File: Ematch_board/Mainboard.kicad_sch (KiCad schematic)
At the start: 69 parts, among them J10 Conn_01x02_Male, J11 Conn_Coaxial, J7 RBUS, J8 USB_C_Receptacle_USB2.0, J9 Conn_01x02_Male, Q1 MMDT2222A, U2 LTC4411, U3 RT9025-25GSP, U4 LTC4411, U5 SN65HVD230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

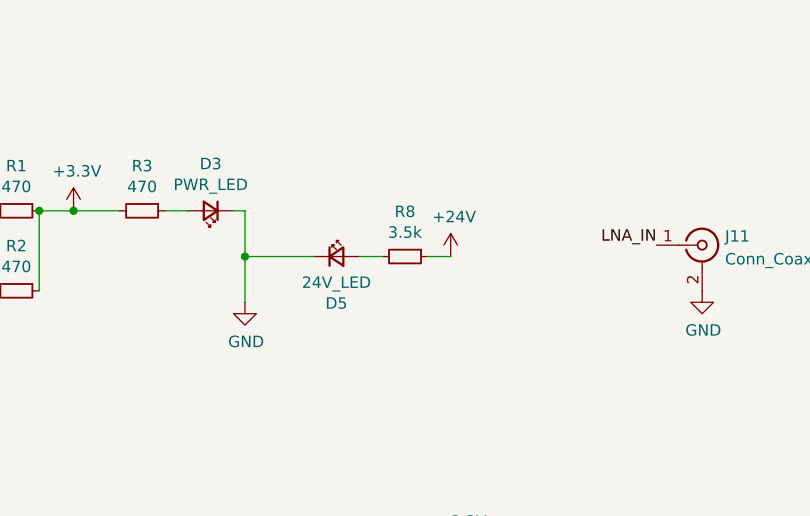
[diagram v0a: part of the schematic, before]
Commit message: Changed 24V LED resistor value
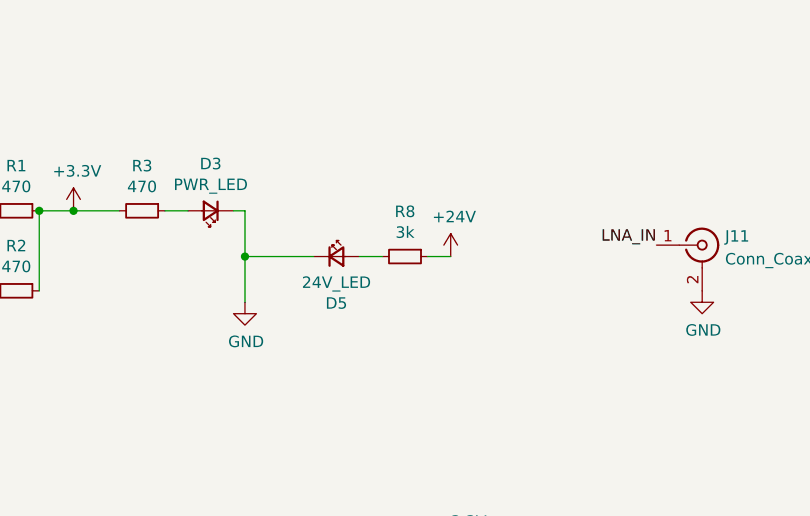
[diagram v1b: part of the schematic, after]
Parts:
- R8: value 3.5k -> 3k
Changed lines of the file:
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@@
     (in_bom yes) (on_board yes)
     (property "Reference" "R8" (id 0) (at 76.2 17.8816 90))
-    (property "Value" "3.5k" (id 1) (at 76.2 20.193 90))
+    (property "Value" "3k" (id 1) (at 76.2 20.193 90))
     (property "Footprint" "Resistor_SMD:R_0603_1608Metric" (id 2) (at 76.2 22.86 0)
       (effects (font (size 1.27 1.27)) hide)
@@
     )
     (path "/9f59f317-c728-437e-b7e8-8cd5c58754eb"
-      (reference "R8") (unit 1) (value "3.5k") (footprint "Resistor_SMD:R_0603_1608Metric")
+      (reference "R8") (unit 1) (value "3k") (footprint "Resistor_SMD:R_0603_1608Metric")
     )
     (path "/2e54b3a5-ce43-4593-88d5-e0f9c220138c"

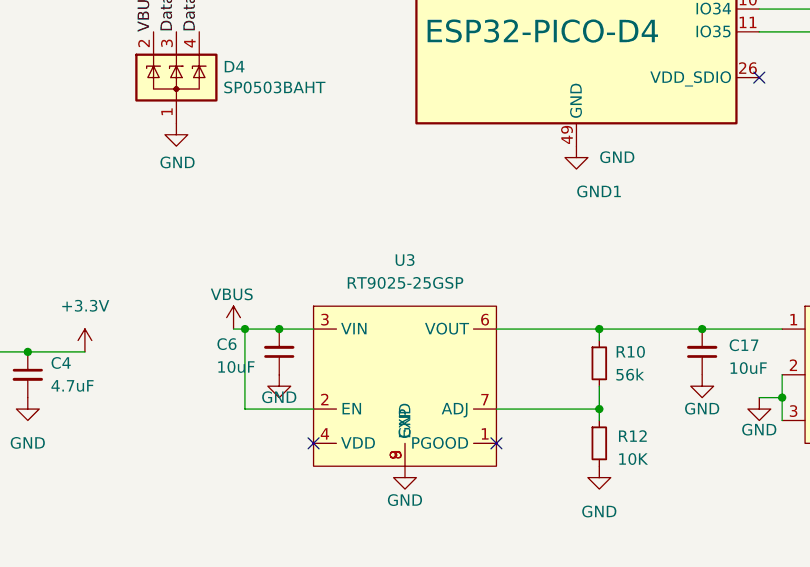
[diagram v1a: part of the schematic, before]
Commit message: Changed LDO symbol
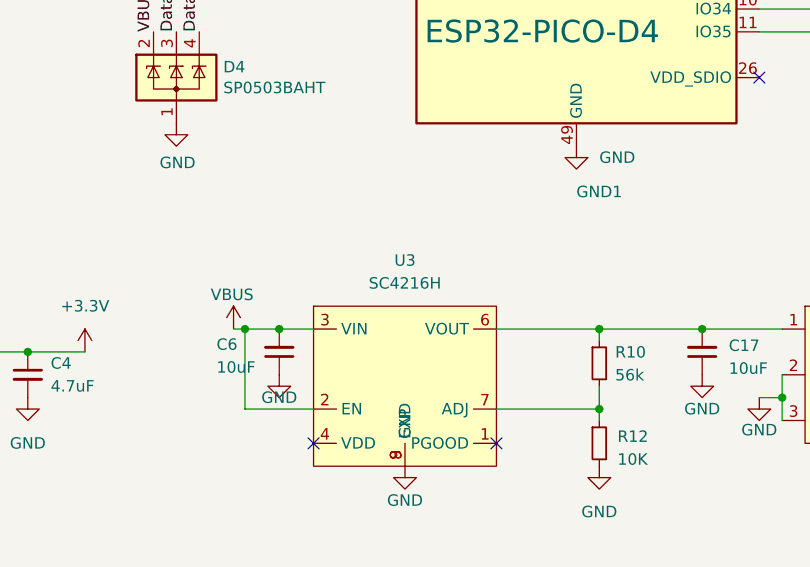
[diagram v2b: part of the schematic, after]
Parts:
- U3: value RT9025-25GSP -> SC4216H
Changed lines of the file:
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@@
     (in_bom yes) (on_board yes) (fields_autoplaced)
     (property "Reference" "U3" (id 0) (at 85.09 160.02 0))
-    (property "Value" "RT9025-25GSP" (id 1) (at 85.09 162.56 0))
+    (property "Value" "SC4216H" (id 1) (at 85.09 162.56 0))
     (property "Footprint" "iclr:SOIC127P599X175-9N" (id 2) (at 85.09 161.29 0)
       (effects (font (size 1.27 1.27)) hide)
@@
     )
     (path "/79f9859b-6f0f-4b8d-bc64-43efc8037e4c"
-      (reference "U3") (unit 1) (value "RT9025-25GSP") (footprint "iclr:SOIC127P599X175-9N")
+      (reference "U3") (unit 1) (value "SC4216H") (footprint "iclr:SOIC127P599X175-9N")
     )
     (path "/f4b8df4e-cc6e-426d-b25b-296487d3b549"

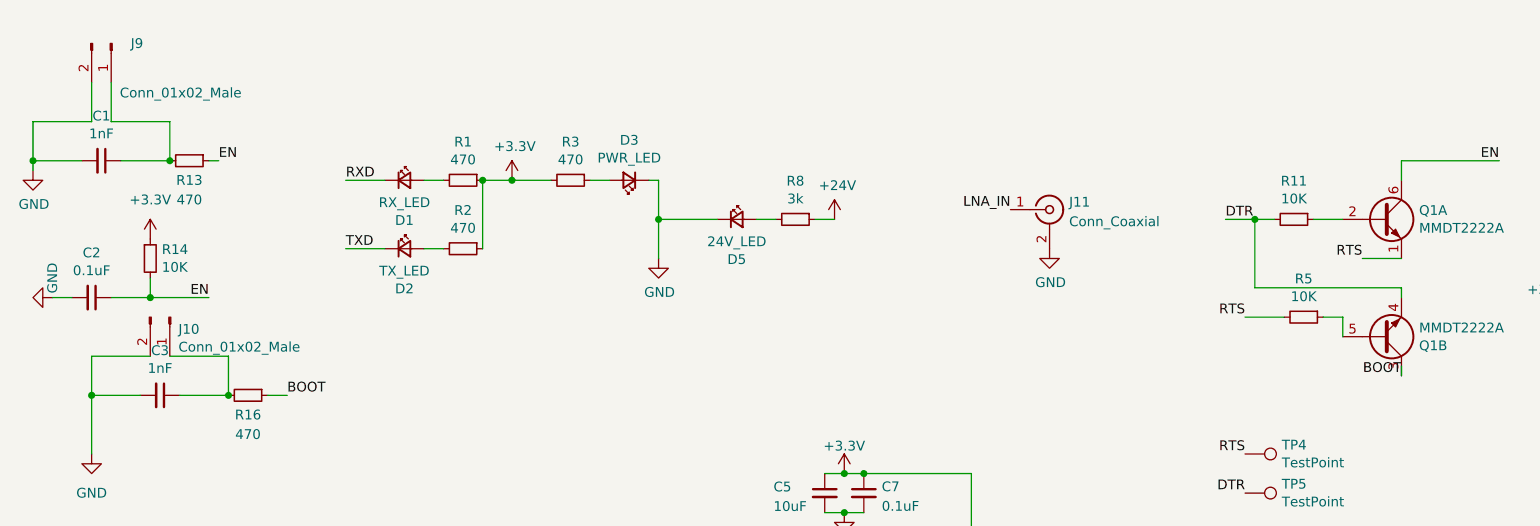
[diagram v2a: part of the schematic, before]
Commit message: Changed boot and EN jumper caps
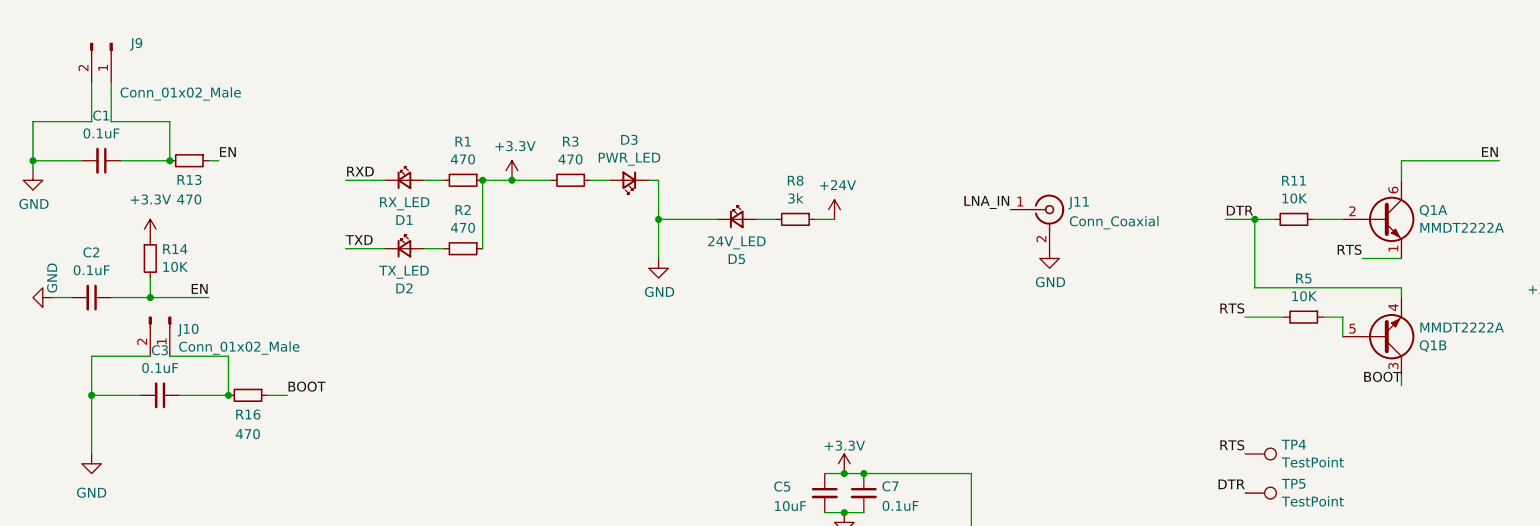
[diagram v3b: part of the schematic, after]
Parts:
- C1, C3: value 1nF -> 0.1uF
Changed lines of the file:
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@@
-    (stroke (width 0) (type default) (color 0 0 0 0))
-  )
-  (wire (pts (xy 154.94 41.91) (xy 154.94 43.18))
     (stroke (width 0) (type default) (color 0 0 0 0))
   )
@@
   )
   (wire (pts (xy 184.15 162.56) (xy 184.15 154.94))
+    (stroke (width 0) (type default) (color 0 0 0 0))
+  )
+  (wire (pts (xy 154.94 44.45) (xy 154.94 43.18))
     (stroke (width 0) (type default) (color 0 0 0 0))
   )
@@
     (effects (font (size 1.27 1.27)) (justify right bottom))
   )
-  (label "BOOT" (at 154.94 43.18 180)
+  (label "BOOT" (at 154.94 44.45 180)
     (effects (font (size 1.27 1.27)) (justify right bottom))
   )
@@
     (in_bom yes) (on_board yes)
     (property "Reference" "C3" (id 0) (at -6.35 39.9034 90))
-    (property "Value" "1nF" (id 1) (at -6.35 42.2148 90))
+    (property "Value" "0.1uF" (id 1) (at -6.35 42.2148 90))
     (property "Footprint" "Capacitor_SMD:C_0603_1608Metric" (id 2) (at -6.35 45.72 0)
       (effects (font (size 1.27 1.27)) hide)
@@
     (in_bom yes) (on_board yes)
     (property "Reference" "C1" (id 0) (at -13.97 9.4234 90))
-    (property "Value" "1nF" (id 1) (at -13.97 11.7348 90))
+    (property "Value" "0.1uF" (id 1) (at -13.97 11.7348 90))
     (property "Footprint" "Capacitor_SMD:C_0603_1608Metric" (id 2) (at -13.97 15.24 0)
       (effects (font (size 1.27 1.27)) hide)
@@
     )
     (path "/00000000-0000-0000-0000-00005dabbfe7"
-      (reference "C1") (unit 1) (value "1nF") (footprint "Capacitor_SMD:C_0603_1608Metric")
+      (reference "C1") (unit 1) (value "0.1uF") (footprint "Capacitor_SMD:C_0603_1608Metric")
     )
     (path "/7468b08c-11d4-40e8-94cc-5b8536475a97"
@@
     )
     (path "/00000000-0000-0000-0000-00005dab5946"
-      (reference "C3") (unit 1) (value "1nF") (footprint "Capacitor_SMD:C_0603_1608Metric")
+      (reference "C3") (unit 1) (value "0.1uF") (footprint "Capacitor_SMD:C_0603_1608Metric")
     )
     (path "/3d0c5cc1-3a97-4ec3-9ebe-7262bf5dcc3c"

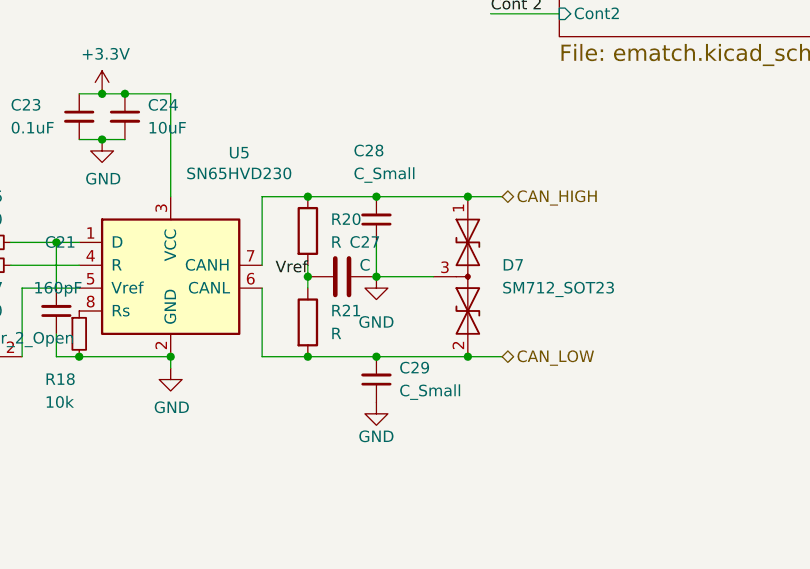
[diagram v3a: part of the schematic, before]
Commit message: set values for can passives
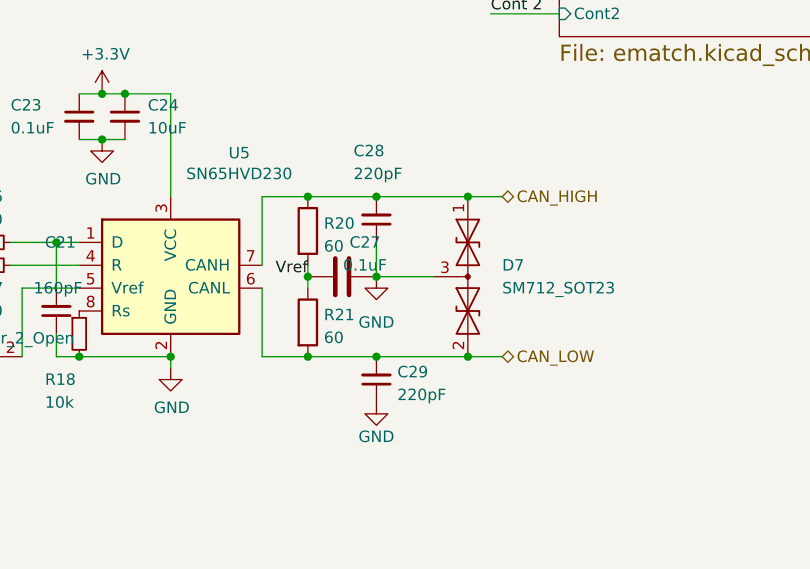
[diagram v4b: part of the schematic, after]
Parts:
- C27: value C -> 0.1uF
- C28, C29: value C_Small -> 220pF
- R20, R21: value R -> 60
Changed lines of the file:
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@@
   (symbol (lib_id "Device:R") (at 215.9 158.75 0) (unit 1)
     (in_bom yes) (on_board yes) (fields_autoplaced)
-    (property "Reference" "R21" (id 0) (at 218.44 157.4799 0)
-      (effects (font (size 1.27 1.27)) (justify left))
-    )
-    (property "Value" "R" (id 1) (at 218.44 160.0199 0)
+    (property "Reference" "R21" (id 0) (at 217.678 157.9153 0)
+      (effects (font (size 1.27 1.27)) (justify left))
+    )
+    (property "Value" "60" (id 1) (at 217.678 160.4522 0)
       (effects (font (size 1.27 1.27)) (justify left))
     )
@@
   (symbol (lib_id "Device:C_Small") (at 223.52 165.1 180) (unit 1)
     (in_bom yes) (on_board yes) (fields_autoplaced)
-    (property "Reference" "C29" (id 0) (at 226.06 163.8235 0)
-      (effects (font (size 1.27 1.27)) (justify right))
-    )
-    (property "Value" "C_Small" (id 1) (at 226.06 166.3635 0)
+    (property "Reference" "C29" (id 0) (at 225.8441 164.2589 0)
+      (effects (font (size 1.27 1.27)) (justify right))
+    )
+    (property "Value" "220pF" (id 1) (at 225.8441 166.7958 0)
       (effects (font (size 1.27 1.27)) (justify right))
     )
@@
     (in_bom yes) (on_board yes)
     (property "Reference" "C27" (id 0) (at 222.25 149.86 90))
-    (property "Value" "C" (id 1) (at 222.25 152.4 90))
+    (property "Value" "0.1uF" (id 1) (at 222.25 152.4 90))
     (property "Footprint" "Capacitor_SMD:C_0603_1608Metric" (id 2) (at 223.52 152.7048 0)
       (effects (font (size 1.27 1.27)) hide)
@@
   (symbol (lib_id "Device:R") (at 215.9 148.59 0) (unit 1)
     (in_bom yes) (on_board yes) (fields_autoplaced)
-    (property "Reference" "R20" (id 0) (at 218.44 147.3199 0)
-      (effects (font (size 1.27 1.27)) (justify left))
-    )
-    (property "Value" "R" (id 1) (at 218.44 149.8599 0)
+    (property "Reference" "R20" (id 0) (at 217.678 147.7553 0)
+      (effects (font (size 1.27 1.27)) (justify left))
+    )
+    (property "Value" "60" (id 1) (at 217.678 150.2922 0)
       (effects (font (size 1.27 1.27)) (justify left))
     )
@@
       (effects (font (size 1.27 1.27)) (justify right))
     )
-    (property "Value" "C_Small" (id 1) (at 220.98 142.24 0)
+    (property "Value" "220pF" (id 1) (at 220.98 142.24 0)
       (effects (font (size 1.27 1.27)) (justify right))
     )
@@
     )
     (path "/b1de2198-1998-4a42-91df-14b52e80383a"
-      (reference "C27") (unit 1) (value "C") (footprint "Capacitor_SMD:C_0603_1608Metric")
+      (reference "C27") (unit 1) (value "0.1uF") (footprint "Capacitor_SMD:C_0603_1608Metric")
     )
     (path "/fb3e282f-807e-451d-a2ae-18e98dba54e8"
-      (reference "C28") (unit 1) (value "C_Small") (footprint "Capacitor_SMD:C_0603_1608Metric")
+      (reference "C28") (unit 1) (value "220pF") (footprint "Capacitor_SMD:C_0603_1608Metric")
     )
     (path "/306bdd76-b4ff-4faa-b4d4-5772a8b99af4"
-      (reference "C29") (unit 1) (value "C_Small") (footprint "Capacitor_SMD:C_0603_1608Metric")
+      (reference "C29") (unit 1) (value "220pF") (footprint "Capacitor_SMD:C_0603_1608Metric")
     )
     (path "/dfb2924b-88e7-4ec5-ace2-e873866fe72c"
@@
     )
     (path "/c518a40c-d5ea-44b0-9013-1ef9c96e186b"
-      (reference "R20") (unit 1) (value "R") (footprint "Resistor_SMD:R_0603_1608Metric")
+      (reference "R20") (unit 1) (value "60") (footprint "Resistor_SMD:R_0603_1608Metric")
     )
     (path "/2dbb9741-f549-40ee-9a94-cc6b63bce1f3"
-      (reference "R21") (unit 1) (value "R") (footprint "Resistor_SMD:R_0603_1608Metric")
+      (reference "R21") (unit 1) (value "60") (footprint "Resistor_SMD:R_0603_1608Metric")
     )
     (path "/bc168c84-c145-4b8c-b46f-63b76f72078c"

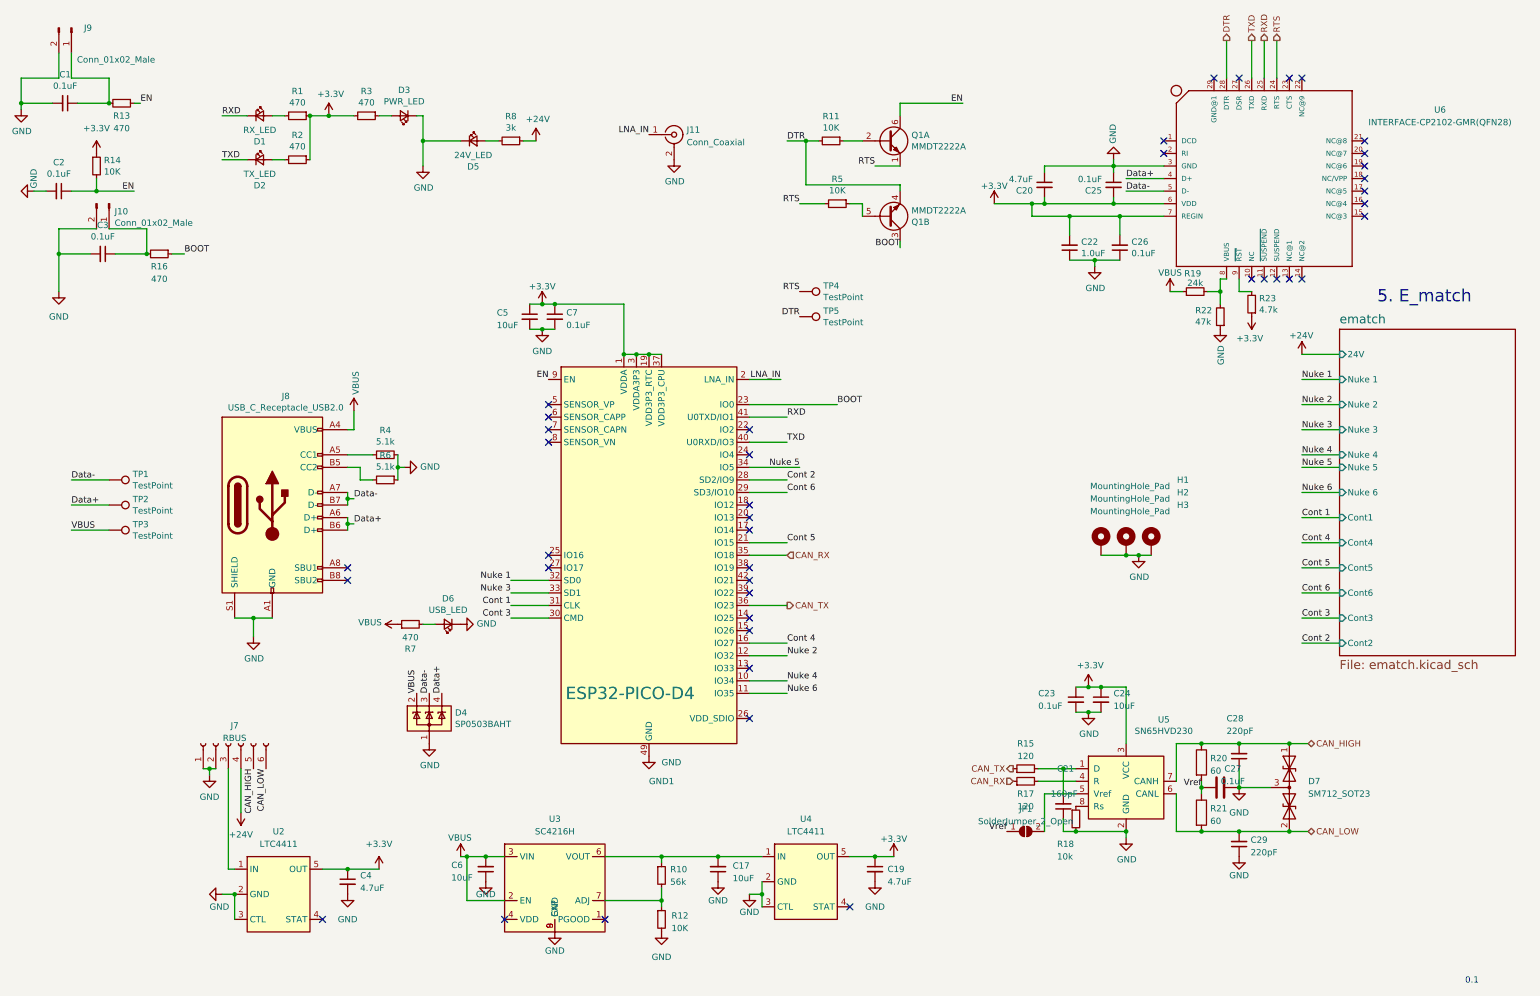
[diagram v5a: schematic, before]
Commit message: moved nuke channels from input only pins, changed resistor values
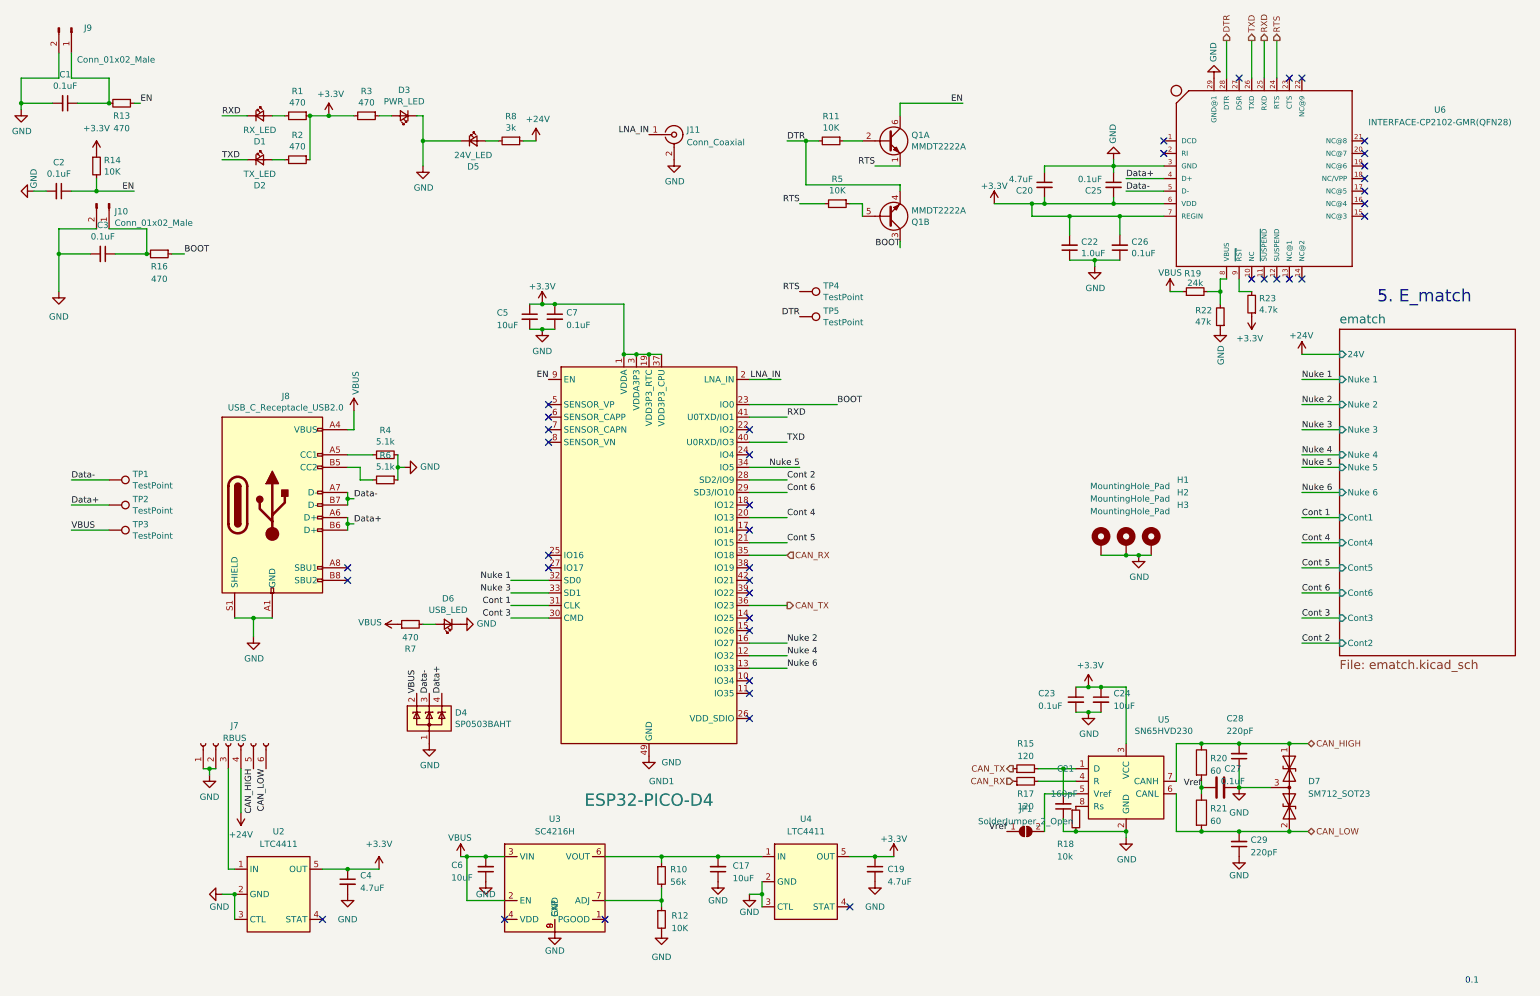
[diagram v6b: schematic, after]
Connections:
- net Cont 4: now also GND1.20 (IO13); no longer GND1.16 (IO27)
- net GND: now also U6.29 (GND@1)
- net Nuke 2: now also GND1.16 (IO27); no longer GND1.12 (IO32)
- net Nuke 4: now also GND1.12 (IO32); no longer GND1.10 (IO34)
- net Nuke 6: now also GND1.13 (IO33); no longer GND1.11 (IO35)
- no-connect marks 42 -> 41
